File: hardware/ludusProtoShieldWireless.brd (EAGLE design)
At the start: 59.7 x 53.3 mm, 72 parts, among them Q1 MOSFET-NCHANNELBSS138, Q2 MOSFET-NCHANNELBSS138, U1 ARDUINO, U3 TB6612FNG

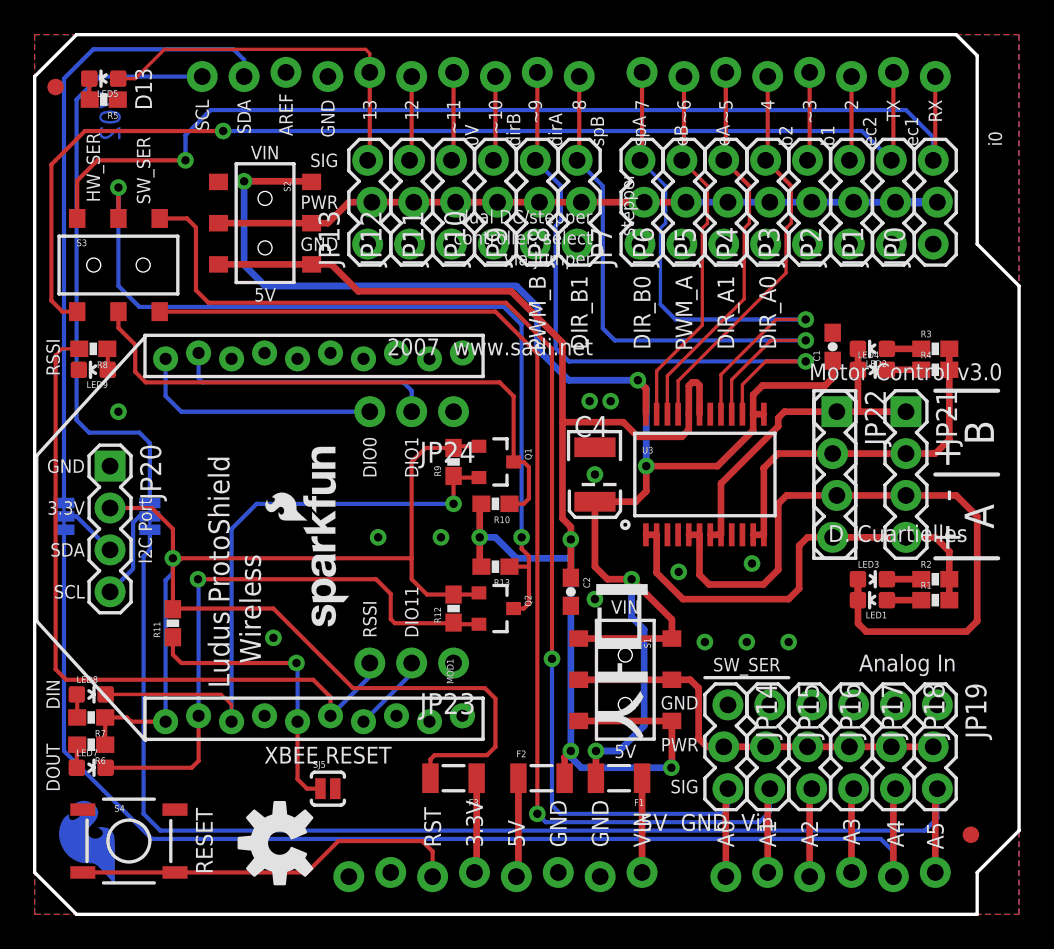
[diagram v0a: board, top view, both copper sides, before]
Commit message: Updated all issues in SCH.
Also, replaced the switch for the DPDT package.
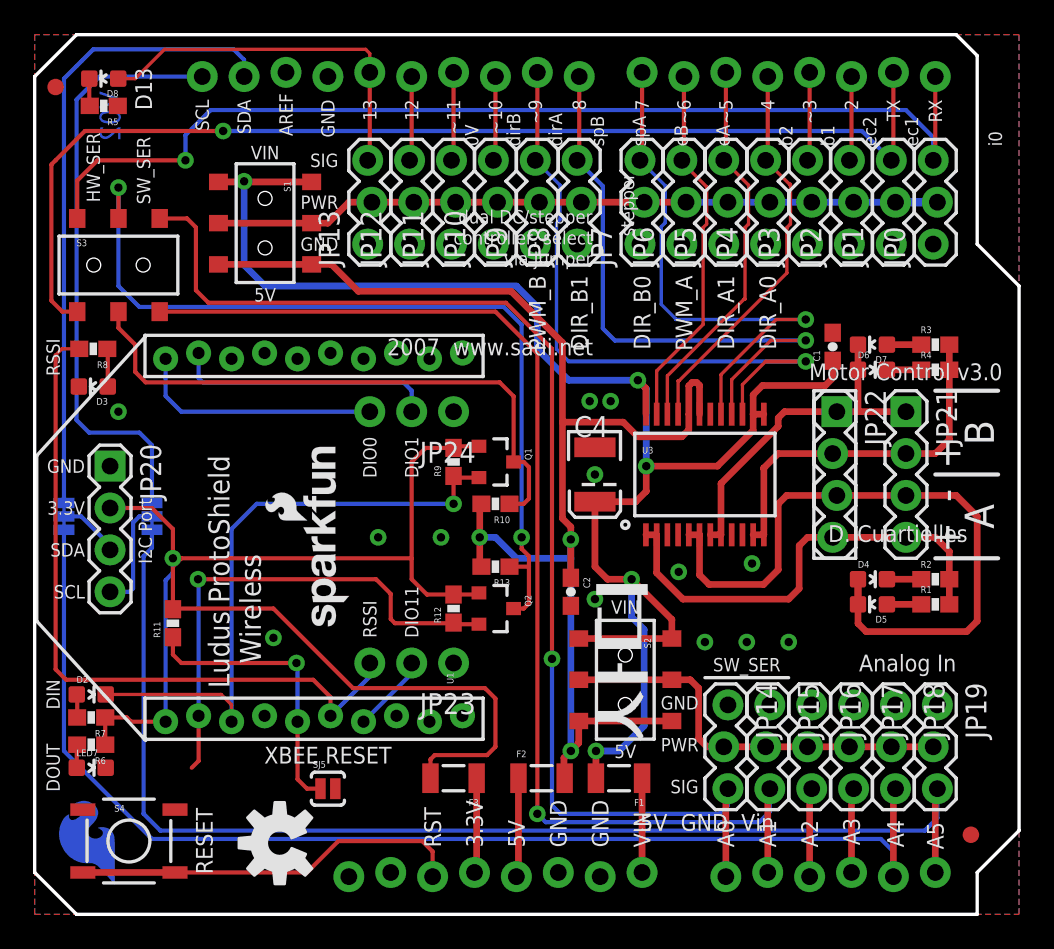
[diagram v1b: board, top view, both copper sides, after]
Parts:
- removed LED1, LED2: Yellow, SparkFun-LED:LED-0603
- removed LED9: Green, SparkFun-LED:LED-0603
- removed MOD1: XBEE-1XBEE-1_LOCK, SparkFun-RF:XBEE-1_LOCK
- added D3: Green, SparkFun-LED:LED-0603
- added D5, D7: Yellow, SparkFun-LED:LED-0603
- added U2: ARDUINO, SparkFun-Boards:UNO_R3_SHIELD_NOLABELS_LOCK
- U1: value ARDUINO -> XBEE-1XBEE-1_LOCK; device SparkFun-Boards:UNO_R3_SHIELD_NOLABELS_LOCK -> SparkFun-RF:XBEE-1_LOCK
- moved U1 41.3 mm to (27.9, 22.9), turned to 90 degrees
- moved S1 35.3 mm to (14.0, 41.9)
- moved S2 35.3 mm to (35.8, 14.2)
- moved R5 0.38 mm to (4.19, 49.0)
- moved R1 0.25 mm to (54.6, 18.8)
- moved R3 0.25 mm to (54.6, 34.5)
- moved SJ4 0.13 mm to (7.11, 24.1)
- renumbered LED3 to D4, LED4 to D6, LED5 to D8, LED8 to D2
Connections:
- new net D1: LED7.C
- net 3.3V: now also U2.3.3V; no longer U1.3.3V
- net 5V: now also U2.5V; no longer U1.5V
- net A0/SW_RXI: now also U2.A0; no longer U1.A0
- net A1/SW_TXO: now also U2.A1; no longer U1.A1
- net A2: now also U2.A2; no longer U1.A2
- net A3: now also U2.A3; no longer U1.A3
- net A4: now also U2.A4; no longer U1.A4
- net A5: now also U2.A5; no longer U1.A5
- net AIN1: now also U2.D4; no longer U1.D4
- net AIN2: now also U2.D5; no longer U1.D5
- net ANALOG_PWR_RAIL: now also S2.2, S2.5; no longer S1.2
- net AOUT2: now also D5.C; no longer LED1.C
- net BIN1: now also U2.D7; no longer U1.D7
- net BIN2: now also U2.D8; no longer U1.D8
- net BOUT2: now also D7.C; no longer LED2.C
- net D0/RXI: now also U2.RX; no longer U1.RX
- net D1/TXO: now also U2.TX; no longer U1.TX
- net D10: now also U2.D10; no longer U1.D10
- net D11: now also U2.D11; no longer U1.D11
- net D12: now also U2.D12; no longer U1.D12
- net D13: now also U2.D13; no longer U1.D13
- net D2: now also U2.D2; no longer U1.D2
- net D3: now also U2.D3; no longer U1.D3
- net DIN: now also U1.3; no longer MOD1.3
- net DIO0: now also U1.20; no longer MOD1.20
- net DIO1: now also U1.19; no longer MOD1.19
- net DIO11: now also U1.7; no longer MOD1.7
- net DOUT: now also U1.2; no longer LED7.C, MOD1.2
- net FUSED_3.3V: now also U1.1; no longer MOD1.1
- net FUSED_5V: now also S1.6, S2.6
- net FUSED_VIN: now also S1.4, S2.4
- net GND: now also D3.C, U1.10, U2.GND@0, U2.GND@1, U2.GND@2; no longer LED9.C, MOD1.10, U1.GND@0, U1.GND@1, U1.GND@2
- net N$3: now also D5.A; no longer LED1.A
- net N$44: now also D3.A; no longer LED9.A
- net N$8: now also D7.A; no longer LED2.A
- net PWMA: now also U2.D6; no longer U1.D6
- net PWMB: now also U2.D9; no longer U1.D9
- net PWR_RAIL: now also S1.2, S1.5; no longer S2.2
- net RESET: now also U2.RES; no longer U1.RES
- net RSSI: now also U1.6; no longer MOD1.6
- net SCL: now also U2.SCL; no longer U1.SCL
- net SDA: now also U2.SDA; no longer U1.SDA
- net VIN: now also U2.VIN; no longer U1.VIN
- net XBEE_RESET: now also U1.5; no longer MOD1.5
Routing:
- net FUSED_VIN: track 92.0 -> 99.3 mm
- net PWR_RAIL: track 38.5 -> 44.1 mm
- net ANALOG_PWR_RAIL: track 19.3 -> 25.0 mm
- net N$6: track 5.59 -> 0.00 mm
- net N$11: track 5.59 -> 0.00 mm
- net N$2: track 5.46 -> 0.00 mm
- net N$4: track 5.33 -> 0.00 mm
- net N$10: track 5.33 -> 0.00 mm
- net DOUT: track 35.9 -> 30.7 mm
- net FUSED_5V: track 79.3 -> 83.0 mm, vias 4 -> 3
- net N$44: track 1.28 -> 2.30 mm
- net SCL_I2C_PORT: track 5.94 -> 6.77 mm

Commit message: Fixed 2 GND flags and SJ5
Updated nets on SJ5 and GND flags
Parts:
- SJ5: value SOLDERJUMPERNO -> (none)
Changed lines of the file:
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@@
 <attribute name="PROD_ID" value="RES-11150" x="25.4" y="8.255" size="1.778" layer="27" rot="R180" display="off"/>
 </element>
-<element name="SJ5" library="SparkFun-Retired" package="SJ_2S-NO" value="SOLDERJUMPERNO" x="17.78" y="7.62"/>
+<element name="SJ5" library="SparkFun-Retired" package="SJ_2S-NO" value="" x="17.78" y="7.62"/>
 <element name="JP23" library="SparkFun-Connectors" package="1X03_NO_SILK" value="" x="25.4" y="15.24" rot="R180"/>
 <element name="JP24" library="SparkFun-Connectors" package="1X03_NO_SILK" value="" x="25.4" y="30.48" rot="R180"/>

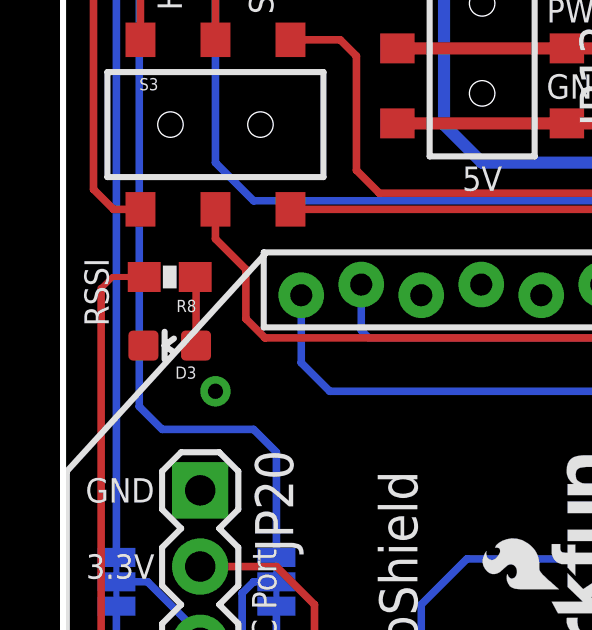
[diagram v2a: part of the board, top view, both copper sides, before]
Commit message: Updating board to include measures and line up silk
Updating board file
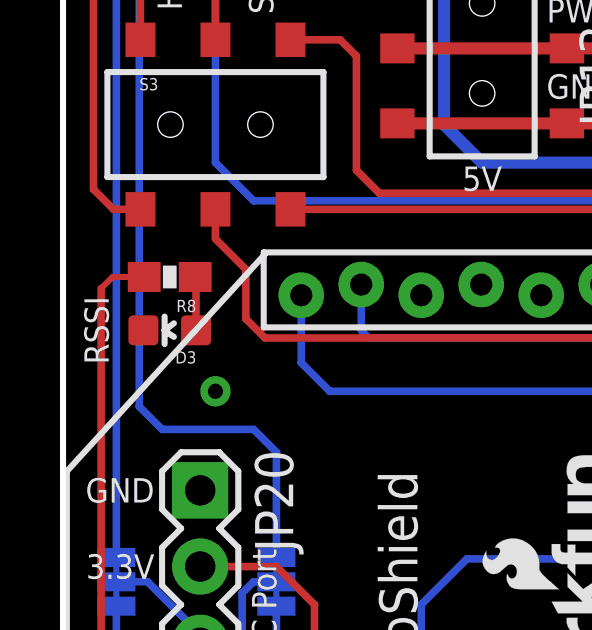
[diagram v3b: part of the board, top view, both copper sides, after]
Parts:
- moved D3 0.51 mm to (3.56, 32.5)
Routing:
- net N$44: track 2.30 -> 1.79 mm
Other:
- board text added: "All measurements are in inches."
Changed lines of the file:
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@@
 <layer number="27" name="tValues" color="7" fill="1" visible="no" active="yes"/>
 <layer number="28" name="bValues" color="7" fill="1" visible="no" active="yes"/>
-<layer number="29" name="tStop" color="7" fill="3" visible="no" active="yes"/>
+<layer number="29" name="tStop" color="7" fill="3" visible="yes" active="yes"/>
 <layer number="30" name="bStop" color="7" fill="6" visible="no" active="yes"/>
 <layer number="31" name="tCream" color="7" fill="4" visible="no" active="yes"/>
@@
 <layer number="45" name="Holes" color="7" fill="1" visible="no" active="yes"/>
 <layer number="46" name="Milling" color="3" fill="1" visible="no" active="yes"/>
-<layer number="51" name="tDocu" color="6" fill="1" visible="no" active="yes"/>
+<layer number="51" name="tDocu" color="6" fill="1" visible="yes" active="yes"/>
 <layer number="52" name="bDocu" color="7" fill="1" visible="no" active="yes"/>
 <layer number="2" name="Route2" color="1" fill="3" visible="no" active="no"/>
@@
 <layer number="37" name="tTest" color="7" fill="1" visible="no" active="no"/>
 <layer number="38" name="bTest" color="7" fill="1" visible="no" active="no"/>
-<layer number="47" name="Measures" color="7" fill="1" visible="no" active="yes"/>
+<layer number="47" name="Measures" color="7" fill="1" visible="yes" active="yes"/>
 <layer number="48" name="Document" color="7" fill="1" visible="no" active="no"/>
 <layer number="49" name="Reference" color="7" fill="1" visible="no" active="no"/>
@@
 <text x="10.795" y="4.445" size="1.016" layer="21" font="vector" ratio="15" rot="R90" align="bottom-center">RESET</text>
 <text x="18.415" y="43.18" size="0.8128" layer="21" font="vector" ratio="15" align="center-right">PWR</text>
-<text x="1.524" y="33.782" size="0.8128" layer="21" font="vector" ratio="15" rot="R270" align="top-center">RSSI</text>
+<text x="1.524" y="32.512" size="0.8128" layer="21" font="vector" ratio="15" rot="R270" align="top-center">RSSI</text>
 <text x="1.524" y="13.335" size="0.8128" layer="21" font="vector" ratio="15" rot="R270" align="top-center">DIN</text>
 <text x="1.524" y="8.89" size="0.8128" layer="21" font="vector" ratio="15" rot="R270" align="top-center">DOUT</text>
@@
 <dimension x1="0" y1="53.34" x2="57.15" y2="50.8" x3="28.575" y3="59.69" textsize="1.778" textratio="15" layer="47" dtype="horizontal" unit="inch"/>
 <dimension x1="57.15" y1="52.07" x2="59.69" y2="38.1" x3="58.42" y3="59.69" textsize="1.778" textratio="15" layer="47" dtype="horizontal" unit="inch"/>
+<text x="-3.81" y="-15.24" size="1.778" layer="47" font="vector" ratio="15">All measurements are in inches.</text>
 </plain>
 <attributes>
@@
 <attribute name="VALUE" value="1K" x="3.429" y="11.938" size="1.778" layer="27" rot="R180" display="off"/>
 </element>
-<element name="D3" library="SparkFun-LED" package="LED-0603" value="Green" x="3.556" y="32.004" rot="R90">
-<attribute name="PROD_ID" value="DIO-00821" x="3.556" y="32.004" size="1.778" layer="27" rot="R90" display="off"/>
-<attribute name="VALUE" value="GREEN" x="3.556" y="32.004" size="1.778" layer="27" rot="R90" display="off"/>
+<element name="D3" library="SparkFun-LED" package="LED-0603" value="Green" x="3.556" y="32.512" rot="R90">
+<attribute name="PROD_ID" value="DIO-00821" x="3.556" y="32.512" size="1.778" layer="27" rot="R90" display="off"/>
+<attribute name="VALUE" value="GREEN" x="3.556" y="32.512" size="1.778" layer="27" rot="R90" display="off"/>
 </element>
 <element name="R8" library="SparkFun-Resistors" package="0603-RES" value="1k" x="3.556" y="34.29" rot="R180">
@@
 <contactref element="D3" pad="A"/>
 <contactref element="R8" pad="1"/>
-<wire x1="4.433" y1="32.004" x2="4.433" y2="34.263" width="0.254" layer="1"/>
+<wire x1="4.433" y1="32.512" x2="4.433" y2="34.263" width="0.254" layer="1"/>
 <wire x1="4.433" y1="34.263" x2="4.406" y2="34.29" width="0.254" layer="1"/>
 </signal>

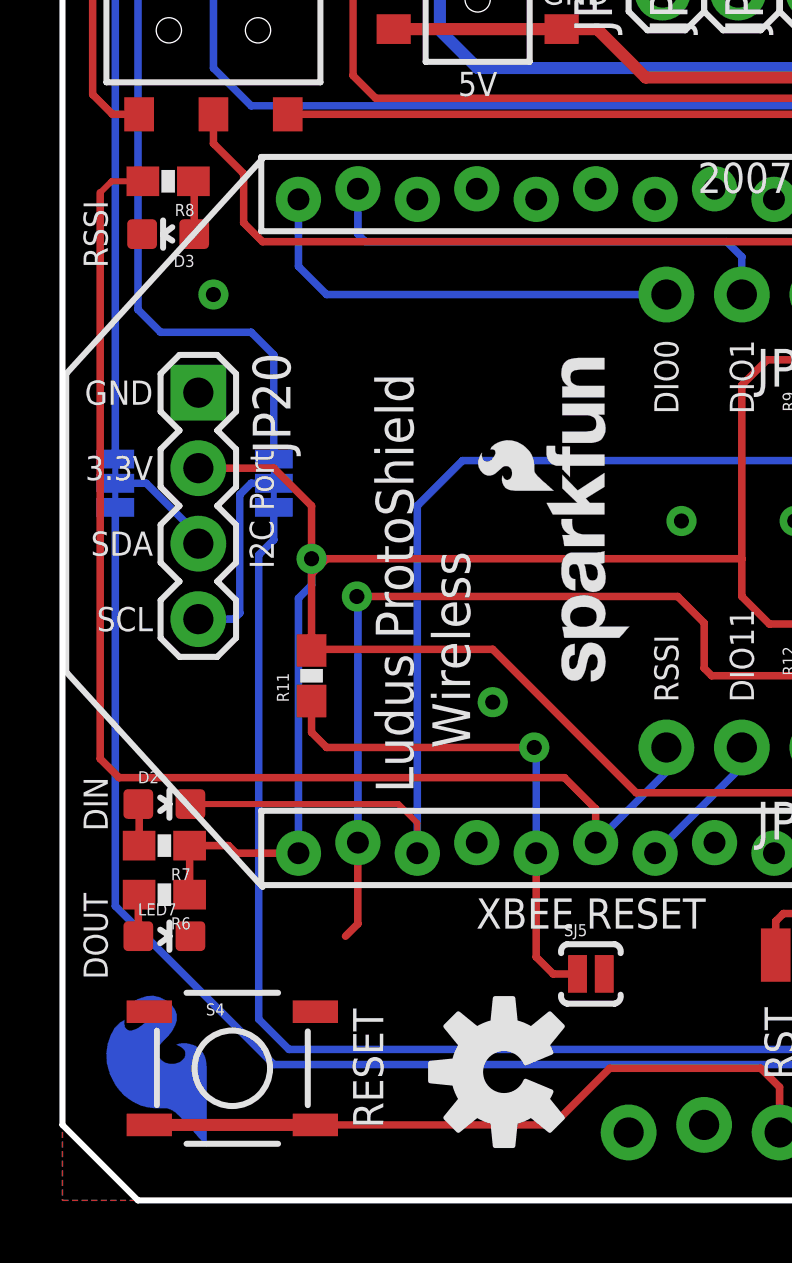
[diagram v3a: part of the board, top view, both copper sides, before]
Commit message: Spaced out LEDs / Resistors
Fixed D1 / DOUT break and spaced out LEDs from resistors
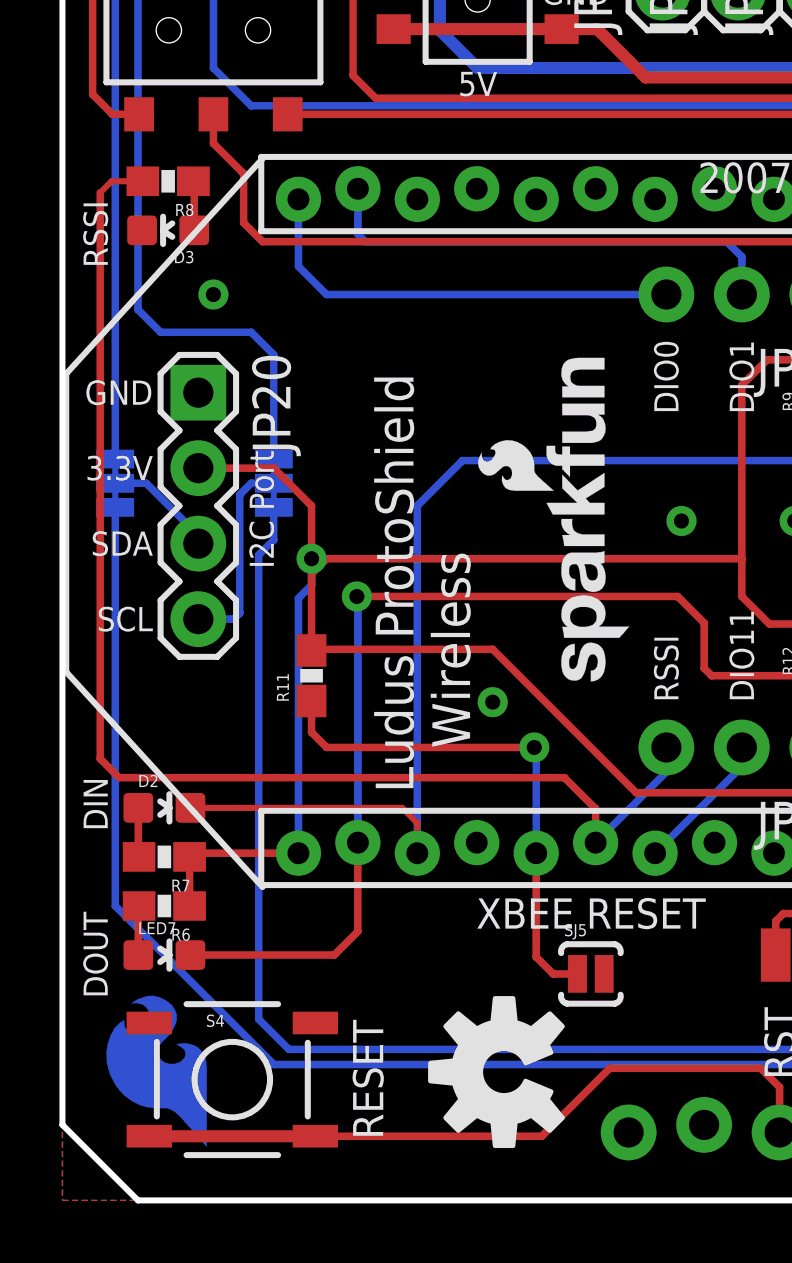
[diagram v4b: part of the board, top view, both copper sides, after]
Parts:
- moved LED7 0.63 mm to (3.43, 8.26)
- moved R6 0.38 mm to (3.43, 9.91)
- moved R7 0.38 mm to (3.43, 11.6)
- moved S4 0.38 mm to (5.71, 4.06)
- moved D3 0.13 mm to (3.56, 32.6)
- moved D2 0.13 mm to (3.43, 13.2)
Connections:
- removed net D1: LED7.C
- net DOUT: now also LED7.C
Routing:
- net DOUT: track 30.7 -> 36.3 mm
